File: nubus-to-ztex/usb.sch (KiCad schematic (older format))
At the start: 13 parts, among them J6 USB micro-B, U6 SN65220, U7 TPS2051C

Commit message: large update
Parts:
- J6: URL https://www.mouser.fr/ProductDetail/Molex/105017-0001?qs=hl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 -> https://lcsc.com/product-detail/USB-Connectors_MOLEX-105017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; URL-ALT (none) -> https://www.mouser.fr/ProductDetail/Molex/105017-0001?qs=hl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
- U6: URL https://www2.mouser.com/ProductDetail/Texas-Instruments/SN6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 -> https://lcsc.com/product-detail/TVS_Texas-Instruments-SN652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; URL-ALT (none) -> https://www2.mouser.com/ProductDetail/Texas-Instruments/SN6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
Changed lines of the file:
@@
 $Descr A4 11693 8268
 encoding utf-8
-Sheet 6 7
+Sheet 5 7
 Title ""
 Date ""
@@
 F 4 "105017-0001" H 5000 2800 50  0001 C CNN "MPN"
 F 5 "Molex" H 5000 2800 50  0001 C CNN "Manufacturer"
-F 6 "https://www.mouser.fr/ProductDetail/Molex/105017-0001?qs=hlXxxvYE36k7QcsR97GUKA%3D%3D" H 5000 2800 50  0001 C CNN "URL"
+F 6 "https://lcsc.com/product-detail/USB-Connectors_MOLEX-1050170001_C136000.html" H 5000 2800 50  0001 C CNN "URL"
+F 7 "https://www.mouser.fr/ProductDetail/Molex/105017-0001?qs=hlXxxvYE36k7QcsR97GUKA%3D%3D" H 5000 2800 50  0001 C CNN "URL-ALT"
 	1    5000 2800
 	-1   0    0    -1
@@
 F 3 "http://www.ti.com/lit/ds/symlink/sn65220.pdf" H 4250 3000 50  0001 C CNN
 F 4 "SN65220DBVR" V 4250 2850 50  0001 C CNN "MPN"
-F 5 "https://www2.mouser.com/ProductDetail/Texas-Instruments/SN65220DBVR?qs=5nGYs9Do7G0gEpYxbYqyeA%3D%3D" V 4250 2850 50  0001 C CNN "URL"
+F 5 "https://www2.mouser.com/ProductDetail/Texas-Instruments/SN65220DBVR?qs=5nGYs9Do7G0gEpYxbYqyeA%3D%3D" V 4250 2850 50  0001 C CNN "URL-ALT"
+F 6 "https://lcsc.com/product-detail/TVS_Texas-Instruments-SN65220DBVR_C21787.html" V 4250 2850 50  0001 C CNN "URL"
 	1    4250 2850
 	0    1    -1   0

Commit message: large clean-up update
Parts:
- U11: renamed from U7; URL https://www.mouser.fr/ProductDetail/Texas-Instruments/TPS20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 -> https://lcsc.com/product-detail/Power-Distribution-Switches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; URL (Mouser) (none) -> https://www.mouser.fr/ProductDetail/Texas-Instruments/TPS20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
- renumbered C16 to C25, C5 to C26, C14 to C27, R9 to R22, R10 to R23, R14 to R24, R15 to R25, R18 to R26, R19 to R27, U6 to U10
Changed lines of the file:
@@
 encoding utf-8
 Sheet 5 7
-Title ""
+Title "nubus-to-ztex USB"
 Date ""
 Rev ""
@@
 	7400 2800 7200 2800
 $Comp
-L power:GND #PWR0179
+L power:GND #PWR0104
 U 1 1 60D9A6B5
 P 6700 3400
-F 0 "#PWR0179" H 6700 3150 50  0001 C CNN
+F 0 "#PWR0104" H 6700 3150 50  0001 C CNN
 F 1 "GND" H 6705 3227 50  0000 C CNN
 F 2 "" H 6700 3400 50  0001 C CNN
@@
 AR Path="/5F679B53/60D9A6C2" Ref="R?"  Part="1"
 AR Path="/5F69F4EF/60D9A6C2" Ref="R?"  Part="1"
-AR Path="/60D72F2C/60D9A6C2" Ref="R19"  Part="1"
-AR Path="/619A5A47/60D9A6C2" Ref="R12"  Part="1"
-AR Path="/61B604DE/60D9A6C2" Ref="R16"  Part="1"
-F 0 "R16" V 6280 2450 50  0000 C CNN
+AR Path="/60D72F2C/60D9A6C2" Ref="R?"  Part="1"
+AR Path="/619A5A47/60D9A6C2" Ref="R?"  Part="1"
+AR Path="/61B604DE/60D9A6C2" Ref="R27"  Part="1"
+F 0 "R27" V 6280 2450 50  0000 C CNN
 F 1 "10k" V 6200 2450 50  0000 C CNN
 F 2 "Resistor_SMD:R_0603_1608Metric" V 6130 2450 50  0001 C CNN
@@
 AR Path="/5F679B53/60D9A6CD" Ref="R?"  Part="1"
 AR Path="/5F69F4EF/60D9A6CD" Ref="R?"  Part="1"
-AR Path="/60D72F2C/60D9A6CD" Ref="R18"  Part="1"
-AR Path="/619A5A47/60D9A6CD" Ref="R11"  Part="1"
-AR Path="/61B604DE/60D9A6CD" Ref="R15"  Part="1"
-F 0 "R15" V 6180 2850 50  0000 C CNN
+AR Path="/60D72F2C/60D9A6CD" Ref="R?"  Part="1"
+AR Path="/619A5A47/60D9A6CD" Ref="R?"  Part="1"
+AR Path="/61B604DE/60D9A6CD" Ref="R26"  Part="1"
+F 0 "R26" V 6180 2850 50  0000 C CNN
 F 1 "10k" V 6100 2850 50  0000 C CNN
 F 2 "Resistor_SMD:R_0603_1608Metric" V 6030 2850 50  0001 C CNN
@@
 AR Path="/5F679B53/60D9A6E1" Ref="C?"  Part="1"
 AR Path="/5F69F4EF/60D9A6E1" Ref="C?"  Part="1"
-AR Path="/60D72F2C/60D9A6E1" Ref="C5"  Part="1"
-AR Path="/619A5A47/60D9A6E1" Ref="C13"  Part="1"
-AR Path="/61B604DE/60D9A6E1" Ref="C17"  Part="1"
-F 0 "C17" H 7225 2100 50  0000 L CNN
+AR Path="/60D72F2C/60D9A6E1" Ref="C?"  Part="1"
+AR Path="/619A5A47/60D9A6E1" Ref="C?"  Part="1"
+AR Path="/61B604DE/60D9A6E1" Ref="C26"  Part="1"
+F 0 "C26" H 7225 2100 50  0000 L CNN
 F 1 "100nF" H 7225 1900 50  0000 L CNN
 F 2 "Capacitor_SMD:C_0603_1608Metric" H 7238 1850 50  0001 C CNN
@@
 $EndComp
 $Comp
-L power:GND #PWR0180
+L power:GND #PWR0105
 U 1 1 60D9A6E8
 P 7200 2150
-F 0 "#PWR0180" H 7200 1900 50  0001 C CNN
+F 0 "#PWR0105" H 7200 1900 50  0001 C CNN
 F 1 "GND" H 7205 1977 50  0000 C CNN
 F 2 "" H 7200 2150 50  0001 C CNN
@@
 	4700 2800 4450 2800
 $Comp
-L Power_Protection:SN65220 U6
+L Power_Protection:SN65220 U10
 U 1 1 60D9A6FD
 P 4250 2850
-F 0 "U6" V 4296 2937 50  0000 L CNN
+F 0 "U10" V 4296 2937 50  0000 L CNN
 F 1 "SN65220" V 4205 2937 50  0000 L CNN
 F 2 "Package_TO_SOT_SMD:SOT-23-6" H 4600 2700 50  0001 L CNN
@@
 	4450 2900 4450 3450
 $Comp
-L power:GND #PWR0181
+L power:GND #PWR0101
 U 1 1 60D9A706
 P 3850 2850
-F 0 "#PWR0181" H 3850 2600 50  0001 C CNN
+F 0 "#PWR0101" H 3850 2600 50  0001 C CNN
 F 1 "GND" H 3855 2677 50  0000 C CNN
 F 2 "" H 3850 2850 50  0001 C CNN
@@
 AR Path="/5F679B53/60D9A70F" Ref="R?"  Part="1"
 AR Path="/5F69F4EF/60D9A70F" Ref="R?"  Part="1"
-AR Path="/60D72F2C/60D9A70F" Ref="R14"  Part="1"
-AR Path="/619A5A47/60D9A70F" Ref="R9"  Part="1"
-AR Path="/61B604DE/60D9A70F" Ref="R13"  Part="1"
-F 0 "R13" V 4030 2500 50  0000 C CNN
+AR Path="/60D72F2C/60D9A70F" Ref="R?"  Part="1"
+AR Path="/619A5A47/60D9A70F" Ref="R?"  Part="1"
+AR Path="/61B604DE/60D9A70F" Ref="R24"  Part="1"
+F 0 "R24" V 4030 2500 50  0000 C CNN
 F 1 "15k" V 3950 2500 50  0000 C CNN
 F 2 "Resistor_SMD:R_0603_1608Metric" V 3880 2500 50  0001 C CNN
@@
 AR Path="/5F679B53/60D9A717" Ref="R?"  Part="1"
 AR Path="/5F69F4EF/60D9A717" Ref="R?"  Part="1"
-AR Path="/60D72F2C/60D9A717" Ref="R15"  Part="1"
-AR Path="/619A5A47/60D9A717" Ref="R10"  Part="1"
-AR Path="/61B604DE/60D9A717" Ref="R14"  Part="1"
-F 0 "R14" V 4030 3200 50  0000 C CNN
+AR Path="/60D72F2C/60D9A717" Ref="R?"  Part="1"
+AR Path="/619A5A47/60D9A717" Ref="R?"  Part="1"
+AR Path="/61B604DE/60D9A717" Ref="R25"  Part="1"
+F 0 "R25" V 4030 3200 50  0000 C CNN
 F 1 "15k" V 3950 3200 50  0000 C CNN
 F 2 "Resistor_SMD:R_0603_1608Metric" V 3880 3200 50  0001 C CNN
@@
 AR Path="/5F679B53/60D9A72D" Ref="R?"  Part="1"
 AR Path="/5F69F4EF/60D9A72D" Ref="R?"  Part="1"
-AR Path="/60D72F2C/60D9A72D" Ref="R9"  Part="1"
-AR Path="/619A5A47/60D9A72D" Ref="R7"  Part="1"
-AR Path="/61B604DE/60D9A72D" Ref="R11"  Part="1"
-F 0 "R11" V 3780 2250 50  0000 C CNN
+AR Path="/60D72F2C/60D9A72D" Ref="R?"  Part="1"
+AR Path="/619A5A47/60D9A72D" Ref="R?"  Part="1"
+AR Path="/61B604DE/60D9A72D" Ref="R22"  Part="1"
+F 0 "R22" V 3780 2250 50  0000 C CNN
 F 1 "27" V 3700 2250 50  0000 C CNN
 F 2 "Resistor_SMD:R_0603_1608Metric" V 3630 2250 50  0001 C CNN
@@
 AR Path="/5F679B53/60D9A735" Ref="R?"  Part="1"
 AR Path="/5F69F4EF/60D9A735" Ref="R?"  Part="1"
-AR Path="/60D72F2C/60D9A735" Ref="R10"  Part="1"
-AR Path="/619A5A47/60D9A735" Ref="R8"  Part="1"
-AR Path="/61B604DE/60D9A735" Ref="R12"  Part="1"
-F 0 "R12" V 3780 3450 50  0000 C CNN
+AR Path="/60D72F2C/60D9A735" Ref="R?"  Part="1"
+AR Path="/619A5A47/60D9A735" Ref="R?"  Part="1"
+AR Path="/61B604DE/60D9A735" Ref="R23"  Part="1"
+F 0 "R23" V 3780 3450 50  0000 C CNN
 F 1 "27" V 3700 3450 50  0000 C CNN
 F 2 "Resistor_SMD:R_0603_1608Metric" V 3630 3450 50  0001 C CNN
@@
 VBus
 $Comp
-L power:GND #PWR0182
+L power:GND #PWR0103
 U 1 1 60D9A747
 P 5000 3200
-F 0 "#PWR0182" H 5000 2950 50  0001 C CNN
+F 0 "#PWR0103" H 5000 2950 50  0001 C CNN
 F 1 "GND" H 5005 3027 50  0000 C CNN
 F 2 "" H 5000 3200 50  0001 C CNN
@@
 	4700 1850 4950 1850
 $Comp
-L Device:CP C16
+L Device:CP C25
 U 1 1 60D9A750
 P 4950 2000
-F 0 "C16" H 5068 2046 50  0000 L CNN
+F 0 "C25" H 5068 2046 50  0000 L CNN
 F 1 "150uF" H 5068 1955 50  0000 L CNN
 F 2 "Capacitor_SMD:C_1206_3216Metric" H 4988 1850 50  0001 C CNN
@@
 	4950 1650 4950 1450
 $Comp
-L power:GND #PWR0183
+L power:GND #PWR0102
 U 1 1 60D9A761
 P 4950 2150
-F 0 "#PWR0183" H 4950 1900 50  0001 C CNN
+F 0 "#PWR0102" H 4950 1900 50  0001 C CNN
 F 1 "GND" H 4955 1977 50  0000 C CNN
 F 2 "" H 4950 2150 50  0001 C CNN
@@
 AR Path="/5F679B53/612D3A06" Ref="C?"  Part="1"
 AR Path="/5F69F4EF/612D3A06" Ref="C?"  Part="1"
-AR Path="/60D72F2C/612D3A06" Ref="C14"  Part="1"
-AR Path="/619A5A47/612D3A06" Ref="C14"  Part="1"
-AR Path="/61B604DE/612D3A06" Ref="C18"  Part="1"
-F 0 "C18" H 7875 2100 50  0000 L CNN
+AR Path="/60D72F2C/612D3A06" Ref="C?"  Part="1"
+AR Path="/619A5A47/612D3A06" Ref="C?"  Part="1"
+AR Path="/61B604DE/612D3A06" Ref="C27"  Part="1"
+F 0 "C27" H 7875 2100 50  0000 L CNN
 F 1 "100nF" H 7875 1900 50  0000 L CNN
 F 2 "Capacitor_SMD:C_0603_1608Metric" H 7888 1850 50  0001 C CNN
@@
 $EndComp
 $Comp
-L power:GND #PWR0184
+L power:GND #PWR0106
 U 1 1 612D3A0D
 P 7850 2150
-F 0 "#PWR0184" H 7850 1900 50  0001 C CNN
+F 0 "#PWR0106" H 7850 1900 50  0001 C CNN
 F 1 "GND" H 7855 1977 50  0000 C CNN
 F 2 "" H 7850 2150 50  0001 C CNN
@@
 VBus
 $Comp
-L Power_Management:TPS2041B U7
+L Power_Management:TPS2041B U11
 U 1 1 60D9A6AC
 P 6700 2800
-F 0 "U7" H 6700 3267 50  0000 C CNN
+F 0 "U11" H 6700 3267 50  0000 C CNN
 F 1 "TPS2051C" H 6700 3176 50  0000 C CNN
 F 2 "Package_TO_SOT_SMD:SOT-23-5" H 6700 3300 50  0001 C CNN
@@
 F 4 "TPS2051CDBVR" H 6700 2800 50  0001 C CNN "MPN"
 F 5 "595-TPS2051CDBVR" H 6700 2800 50  0001 C CNN "Mouser No"
-F 6 "https://www.mouser.fr/ProductDetail/Texas-Instruments/TPS2051CDBVR?qs=PF3AD18CSE5vi2HeWLJCmw%3D%3D" H 6700 2800 50  0001 C CNN "URL"
+F 6 "https://www.mouser.fr/ProductDetail/Texas-Instruments/TPS2051CDBVR?qs=PF3AD18CSE5vi2HeWLJCmw%3D%3D" H 6700 2800 50  0001 C CNN "URL (Mouser)"
+F 7 "https://lcsc.com/product-detail/Power-Distribution-Switches_Texas-Instruments-TPS2051CDBVR_C129581.html" H 6700 2800 50  0001 C CNN "URL"
 	1    6700 2800
 	1    0    0    -1

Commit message: more updates
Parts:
- U10: MPN SN65220DBVR -> SN65220DBVT; Notes (none) -> SN65220DBVT or SN65220DBVR (Tape or Reel...); URL https://lcsc.com/product-detail/TVS_Texas-Instruments-SN652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 -> https://www.lcsc.com/product-detail/Others_Texas-Instrument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
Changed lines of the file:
@@
 F 2 "Package_TO_SOT_SMD:SOT-23-6" H 4600 2700 50  0001 L CNN
 F 3 "http://www.ti.com/lit/ds/symlink/sn65220.pdf" H 4250 3000 50  0001 C CNN
-F 4 "SN65220DBVR" V 4250 2850 50  0001 C CNN "MPN"
+F 4 "SN65220DBVT" V 4250 2850 50  0001 C CNN "MPN"
 F 5 "https://www2.mouser.com/ProductDetail/Texas-Instruments/SN65220DBVR?qs=5nGYs9Do7G0gEpYxbYqyeA%3D%3D" V 4250 2850 50  0001 C CNN "URL-ALT"
-F 6 "https://lcsc.com/product-detail/TVS_Texas-Instruments-SN65220DBVR_C21787.html" V 4250 2850 50  0001 C CNN "URL"
+F 6 "https://www.lcsc.com/product-detail/Others_Texas-Instruments-TI-SN65220DBVT_C350555.html" V 4250 2850 50  0001 C CNN "URL"
+F 7 "SN65220DBVT or SN65220DBVR (Tape or Reel...)" V 4250 2850 50  0001 C CNN "Notes"
 	1    4250 2850
 	0    1    -1   0

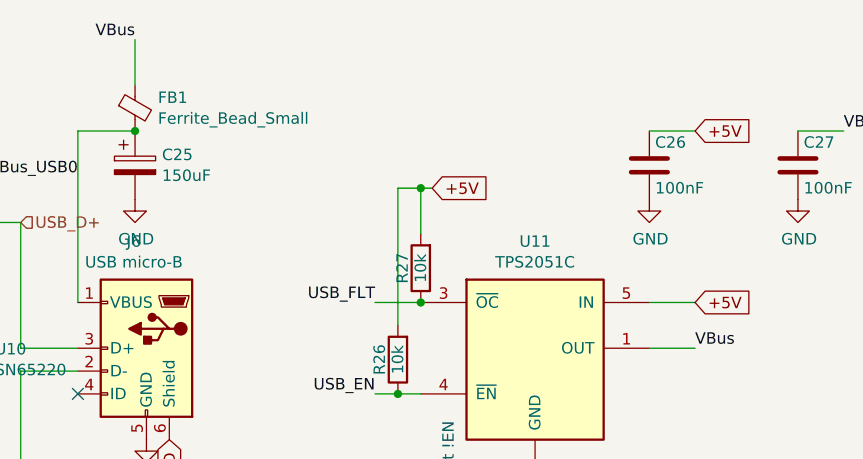
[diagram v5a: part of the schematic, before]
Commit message: merge pmod & leds into an extended pmod on the outside. Also some BoM updates.
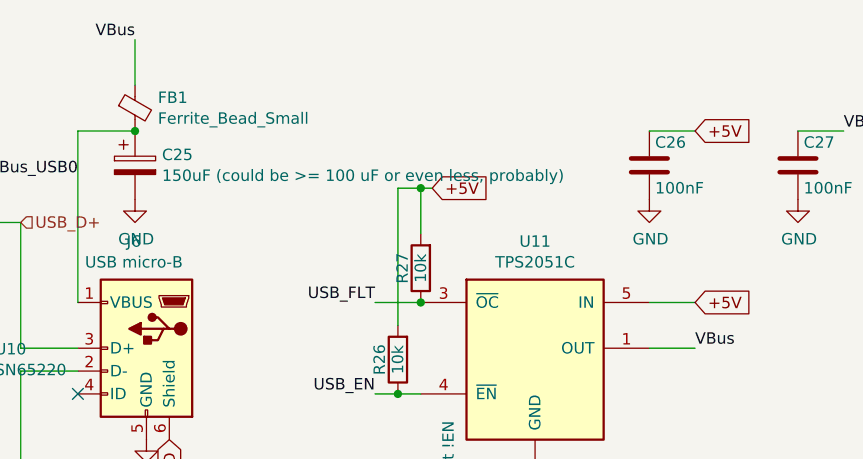
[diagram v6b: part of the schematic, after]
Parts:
- C25: value 150uF -> 150uF (could be >= 100 uF or even less, probably); MPN GRM31CR60J157ME11L -> JMK316ABJ107ML-T; MPN-ALT (none) -> GRM31CR60J157ME11L; URL https://lcsc.com/product-detail/Multilayer-Ceramic-Capacito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 -> https://www.lcsc.com/product-detail/Multilayer-Ceramic-Capa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; URL (mouser) https://www.mouser.fr/ProductDetail/Murata-Electronics/GRM3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 -> (none); URL-ALT (none) -> https://lcsc.com/product-detail/Multilayer-Ceramic-Capacito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; URL-ALT (mouser) (none) -> https://www.mouser.fr/ProductDetail/Murata-Electronics/GRM3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
- C26, C27: URL (none) -> https://lcsc.com/product-detail/Multilayer-Ceramic-Capacito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
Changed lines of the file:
@@
 $Descr A4 11693 8268
 encoding utf-8
-Sheet 5 10
+Sheet 5 9
 Title "nubus-to-ztex USB"
 Date ""
@@
 F 9 "?" H 7200 2000 50  0001 C CNN "Koncar"
 F 10 "TB" H 7200 2000 50  0001 C CNN "Side"
+F 11 "https://lcsc.com/product-detail/Multilayer-Ceramic-Capacitors-MLCC-SMD-SMT_YAGEO-CC0603KRX7R8BB104_C92490.html" H 3000 6050 50  0001 C CNN "URL"
 	1    7200 2000
 	1    0    0    -1
@@
 P 4950 2000
 F 0 "C25" H 5068 2046 50  0000 L CNN
-F 1 "150uF" H 5068 1955 50  0000 L CNN
+F 1 "150uF (could be >= 100 uF or even less, probably)" H 5068 1955 50  0000 L CNN
 F 2 "Capacitor_SMD:C_1206_3216Metric" H 4988 1850 50  0001 C CNN
 F 3 "~" H 4950 2000 50  0001 C CNN
-F 4 "GRM31CR60J157ME11L" H 4950 2000 50  0001 C CNN "MPN"
-F 5 "https://lcsc.com/product-detail/Multilayer-Ceramic-Capacitors-MLCC-SMD-SMT_Murata-Electronics-GRM31CR60J157ME11L_C528968.html" H 4950 2000 50  0001 C CNN "URL"
-F 6 "https://www.mouser.fr/ProductDetail/Murata-Electronics/GRM31CR60J157ME11L?qs=qSv5qXjCIG3a12X8fU8miQ%3D%3D" H 4950 2000 50  0001 C CNN "URL (mouser)"
+F 4 "GRM31CR60J157ME11L" H 4950 2000 50  0001 C CNN "MPN-ALT"
+F 5 "https://lcsc.com/product-detail/Multilayer-Ceramic-Capacitors-MLCC-SMD-SMT_Murata-Electronics-GRM31CR60J157ME11L_C528968.html" H 4950 2000 50  0001 C CNN "URL-ALT"
+F 6 "https://www.mouser.fr/ProductDetail/Murata-Electronics/GRM31CR60J157ME11L?qs=qSv5qXjCIG3a12X8fU8miQ%3D%3D" H 4950 2000 50  0001 C CNN "URL-ALT (mouser)"
+F 7 "JMK316ABJ107ML-T" H 4950 2000 50  0001 C CNN "MPN"
+F 8 "https://www.lcsc.com/product-detail/Multilayer-Ceramic-Capacitors-MLCC-SMD-SMT_Taiyo-Yuden-JMK316ABJ107ML-T_C268006.html" H 4950 2000 50  0001 C CNN "URL"
 	1    4950 2000
 	1    0    0    -1
@@
 F 9 "?" H 7850 2000 50  0001 C CNN "Koncar"
 F 10 "TB" H 7850 2000 50  0001 C CNN "Side"
+F 11 "https://lcsc.com/product-detail/Multilayer-Ceramic-Capacitors-MLCC-SMD-SMT_YAGEO-CC0603KRX7R8BB104_C92490.html" H 3000 6050 50  0001 C CNN "URL"
 	1    7850 2000
 	1    0    0    -1
